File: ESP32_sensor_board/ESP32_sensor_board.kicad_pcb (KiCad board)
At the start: 4 copper layers, 112 x 56.5 mm, 83 parts, among them J1 SS-52400-003, J2 B2B-PH-SM4-TB, J3 GSD090012SEU, J4 Conn_01x04_Pin, J6 Conn_01x05_Pin, Q1 TEMT6000X01, Q2 BC817, Q3 BC817, U1 MCP73871, U2 BME280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

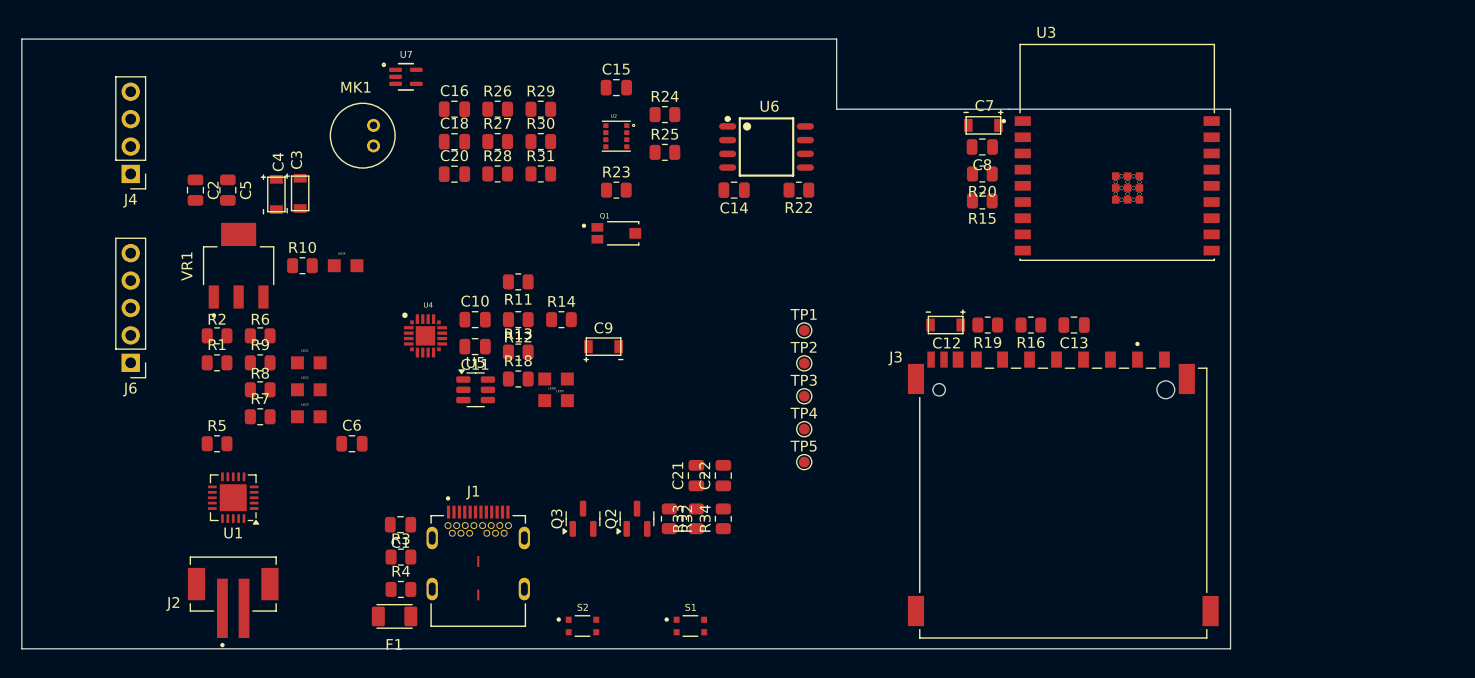
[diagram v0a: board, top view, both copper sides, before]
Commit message: Schematic design C19 added
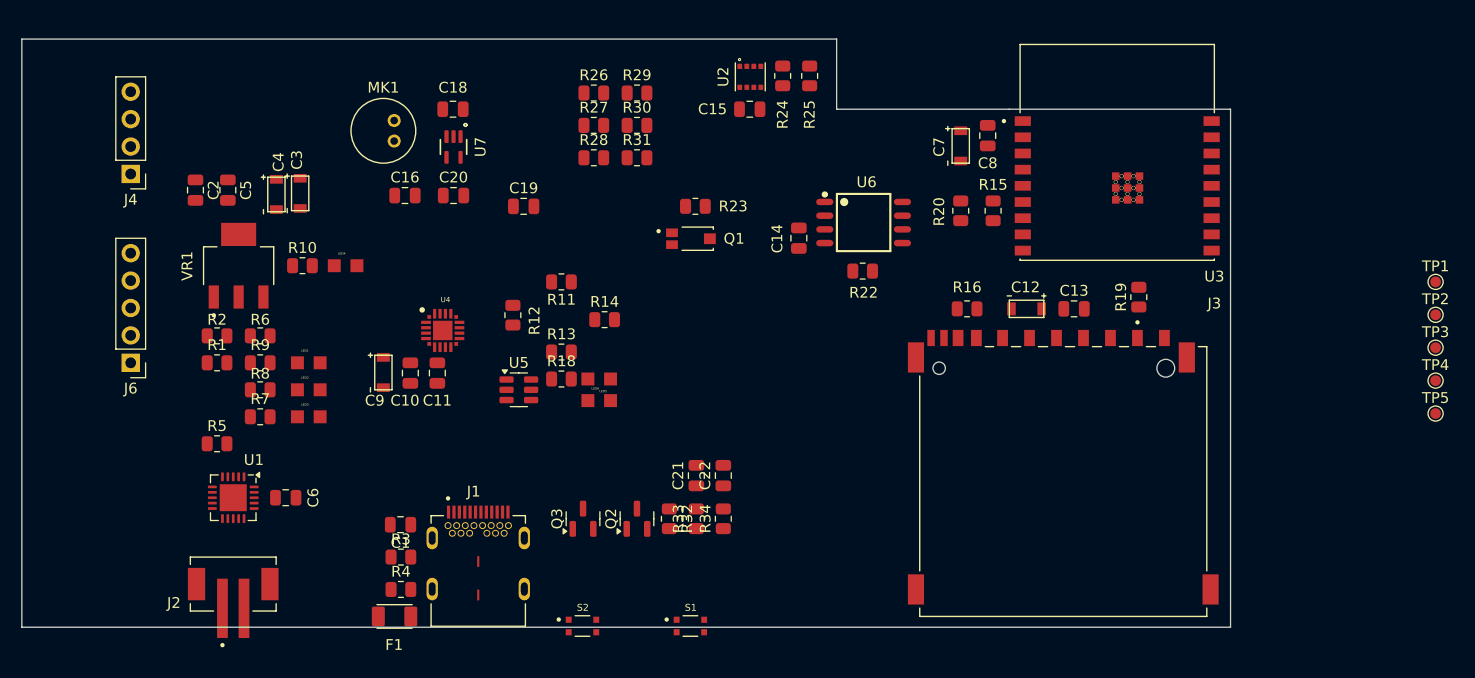
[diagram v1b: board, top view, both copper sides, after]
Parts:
- added C19: 1u, Capacitor_SMD:C_0805_2012Metric, F.Cu at (146.5, 75.5)
- moved TP1 58.7 mm to (231.0, 82.5)
- moved TP2 58.7 mm to (231.0, 85.5)
- moved TP3 58.7 mm to (231.0, 88.6)
- moved TP4 58.7 mm to (231.0, 91.7)
- moved TP5 58.7 mm to (231.0, 94.7)
- moved C9 19.6 mm to (132.7, 89.3), turned to -90 degrees
- moved R25 15.2 mm to (173.0, 63.4), turned to 90 degrees
- moved R19 14.2 mm to (203.5, 83.9), turned to 90 degrees
- moved U2 13.6 mm to (167.5, 63.5), turned to 90 degrees
- moved C15 12.5 mm to (167.4, 66.5)
- moved R24 11.5 mm to (170.5, 63.4), turned to 90 degrees
- moved U6 11.4 mm to (178.0, 77.0)
- moved R22 9.55 mm to (177.9, 81.5)
- moved C16 9.22 mm to (135.5, 74.5)
- moved R26 9.04 mm to (153.0, 65.0)
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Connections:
- net /ESP32-C3-02/Sensors/FEEDBACK renamed /ESP32-C3-02/Sensors/FEEDBACK_1
- R30 pad 2: GND -> /ESP32-C3-02/Sensors/FEEDBACK_2
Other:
- board size 112 x 56.5 mm -> 112 x 54.5 mm

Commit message: Layout design section 2 completed
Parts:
- added C17: 10n, Capacitor_SMD:C_0805_2012Metric, F.Cu at (143.0, 76.5)
- added H1: MountingHole, MountingHole:MountingHole_2.5mm, F.Cu at (177.0, 85.0)
- added H2: MountingHole, MountingHole:MountingHole_2.5mm, F.Cu at (129.0, 73.5)
- added H3: MountingHole, MountingHole:MountingHole_2.5mm, F.Cu at (129.0, 89.5)
- C20: value 0.1u -> 100p
- moved J4 45.4 mm to (154.5, 63.0), turned to -90 degrees
- moved J6 40.3 mm to (140.0, 63.0), turned to -90 degrees
- moved C9 31.8 mm to (164.3, 92.7), turned to 90 degrees
- moved C2 31.4 mm to (141.5, 92.5), turned to 180 degrees
- moved R2 30.1 mm to (145.0, 101.0), turned to -90 degrees
- moved C1 28.0 mm to (162.5, 99.5), turned to -90 degrees
- moved C11 27.5 mm to (166.0, 91.0), turned to 90 degrees
- moved R1 26.8 mm to (142.5, 101.0), turned to -90 degrees
- moved C10 25.0 mm to (161.0, 91.0), turned to 90 degrees
- moved U1 24.4 mm to (143.5, 107.5), turned to 180 degrees
- moved R12 24.3 mm to (167.0, 97.0), turned to 0 degrees
- moved C3 24.2 mm to (142.7, 89.2), turned to 180 degrees
- moved Q3 24.0 mm to (176.0, 103.4)
- moved F1 23.0 mm to (150.5, 97.0)
- moved R6 22.4 mm to (140.0, 101.0), turned to -90 degrees
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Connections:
- MK1 pad OUT: /ESP32-C3-02/Sensors/MK_INPUT -> /ESP32-C3-02/Sensors/MK
- R27 pad 2: /ESP32-C3-02/Sensors/MK_INPUT -> /ESP32-C3-02/Sensors/MK_DC
- R28 pad 2: /ESP32-C3-02/Sensors/MK_INPUT -> /ESP32-C3-02/Sensors/MK
- R29 pad 1: /ESP32-C3-02/Sensors/MK_INPUT -> /ESP32-C3-02/Sensors/MK_DC
- U7 pad 1: /ESP32-C3-02/Sensors/MK_INPUT -> /ESP32-C3-02/Sensors/MK_DC
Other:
- board size 112 x 54.5 mm -> 87 x 54.5 mm

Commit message: Layout design section 3 in progress
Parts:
- moved TP5 57.0 mm to (177.5, 75.0)
- moved TP2 51.5 mm to (180.0, 92.5)
- moved TP1 51.4 mm to (180.0, 88.8)
- moved TP3 47.3 mm to (184.8, 78.8)
- moved TP4 24.6 mm to (207.5, 84.2)
- moved H1 14.3 mm to (170.0, 72.5)
- moved R32 8.37 mm to (167.5, 104.0)
- moved C14 6.67 mm to (171.5, 81.5)
- moved R22 6.67 mm to (177.5, 84.5)
- moved U6 6.67 mm to (177.5, 80.0)
- moved R16 6.52 mm to (181.0, 84.5)
- moved C15 0.50 mm to (166.5, 66.5)
- moved F1 0.50 mm to (150.0, 97.0)
- moved R24 0.50 mm to (169.5, 63.5)
- moved R25 0.50 mm to (172.0, 63.5)
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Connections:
- net Net-(J1-CC1) renamed /CC1
- net Net-(J1-CC2) renamed /CC2
- TP3 pad 1: /ESP32-C3-02/SCLK -> /ESP32-C3-02/CLK
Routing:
- net /ESP32-C3-02/SCL: track 0.00 -> 76.4 mm, vias 0 -> 2
- net /ESP32-C3-02/SDA: track 0.00 -> 76.3 mm, vias 0 -> 2
- net /ESP32-C3-02/MISO_DO: track 0.00 -> 64.2 mm, vias 0 -> 2
- net /ESP32-C3-02/MOSI_DI: track 0.00 -> 56.3 mm
- net /ESP32-C3-02/CS_MEM: track 0.00 -> 43.2 mm, vias 0 -> 2
- net /ESP32-C3-02/CS_SD: track 0.00 -> 26.1 mm, vias 0 -> 2
- net /ESP32-C3-02/CLK: track 0.00 -> 23.2 mm
- net /VBAT: track 0.00 -> 12.0 mm
- net /ESP32-C3-02/DAT0: track 0.00 -> 9.35 mm
- net /ESP32-C3-02/DO: track 0.00 -> 7.40 mm
- net /ESP32-C3-02/SCLK: track 0.00 -> 7.00 mm
- net /ESP32-C3-02/USB_D+: track 0.00 -> 4.61 mm
- net /ESP32-C3-02/USB_D-: track 0.00 -> 4.61 mm
- net /USB_DP: track 0.00 -> 3.03 mm
- net /USB_DN: track 0.00 -> 3.03 mm
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- added copper zone on F.Cu, net +3.3V
- added copper zone on In1.Cu, net +3.3V
- added copper zone on F.Cu, net +5V
- added copper zone on F.Cu, net /+5V_USB
- added copper zone on In1.Cu, net /+5V_USB
- added copper zone on F.Cu, net /VBAT
- added copper zone on F.Cu, net /VBUS
- added copper zone on In1.Cu, net /VBUS
- added copper zone on F.Cu, net GND
- added copper zone on In2.Cu, net GND

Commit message: Layout design section 3 completed
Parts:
- moved TP4 2.15 mm to (206.2, 82.5)
- moved C1 1.68 mm to (161.8, 98.0), turned to 90 degrees
- moved C6 0.50 mm to (143.5, 112.0)
- moved LED1 0.50 mm to (128.0, 97.5)
- moved LED2 0.50 mm to (131.5, 97.5)
- moved LED3 0.50 mm to (135.0, 97.5)
- moved R1 0.50 mm to (142.5, 101.5)
- moved R2 0.50 mm to (145.0, 101.5)
- moved R5 0.50 mm to (137.5, 101.5)
- moved R6 0.50 mm to (140.0, 101.5)
- moved R7 0.50 mm to (135.0, 101.5)
- moved R8 0.50 mm to (131.5, 101.5)
- moved R9 0.50 mm to (128.0, 101.5)
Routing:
- net +5V: track 0.00 -> 33.4 mm
- net GND: track 0.00 -> 32.6 mm, vias 19 -> 35
- net +3.3V: track 0.00 -> 15.6 mm, vias 7 -> 13
- net /VBUS: track 0.00 -> 14.4 mm, vias 3 -> 8
- net /+5V_USB: track 0.00 -> 14.2 mm, vias 3 -> 11
- net /ESP32-C3-02/CS_MEM: track 43.2 -> 41.2 mm
- net /ESP32-C3-02/MISO_DO: track 64.2 -> 65.2 mm, vias 2 -> 0
- net /VBAT: track 12.0 -> 12.9 mm
- net /ESP32-C3-02/SCL: track 76.4 -> 77.1 mm, vias 2 -> 4
- net /ESP32-C3-02/CS_SD: track 26.1 -> 26.4 mm, vias 2 -> 0

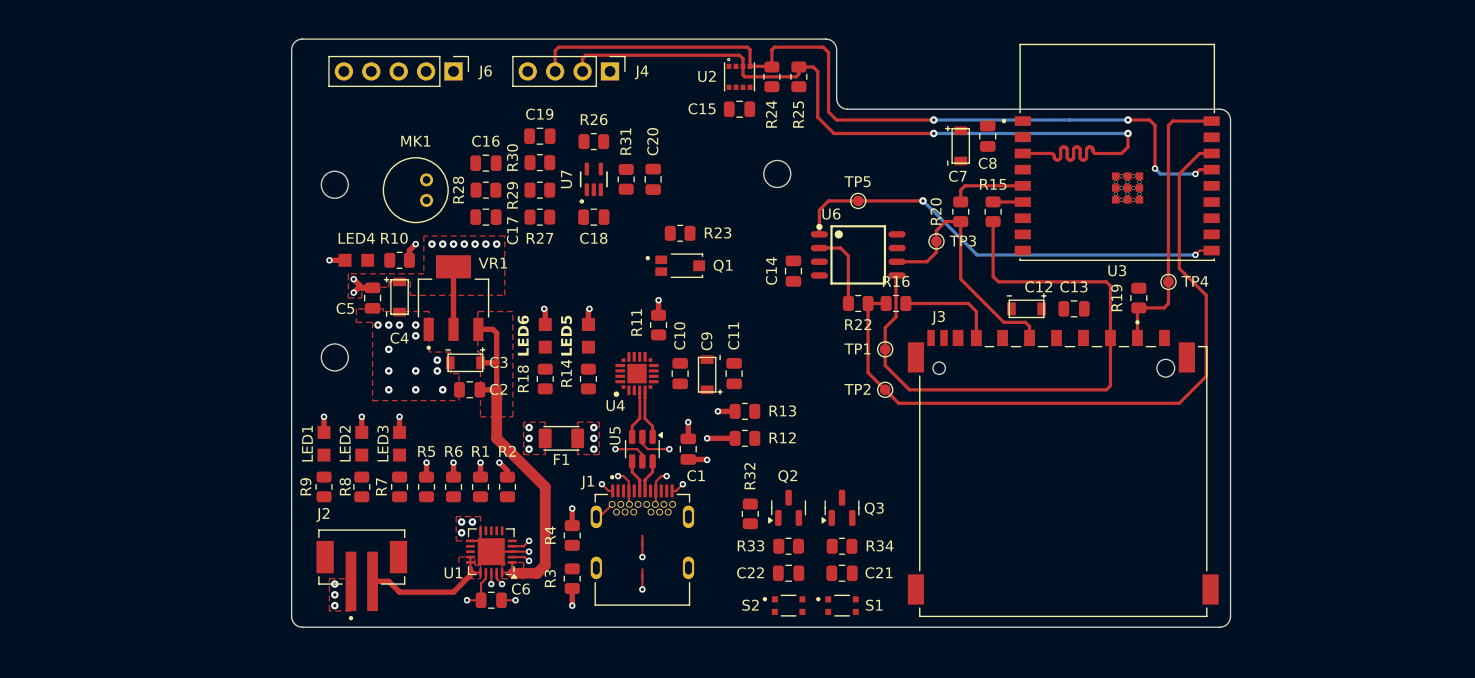
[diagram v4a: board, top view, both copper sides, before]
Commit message: Layout design section 4 completed
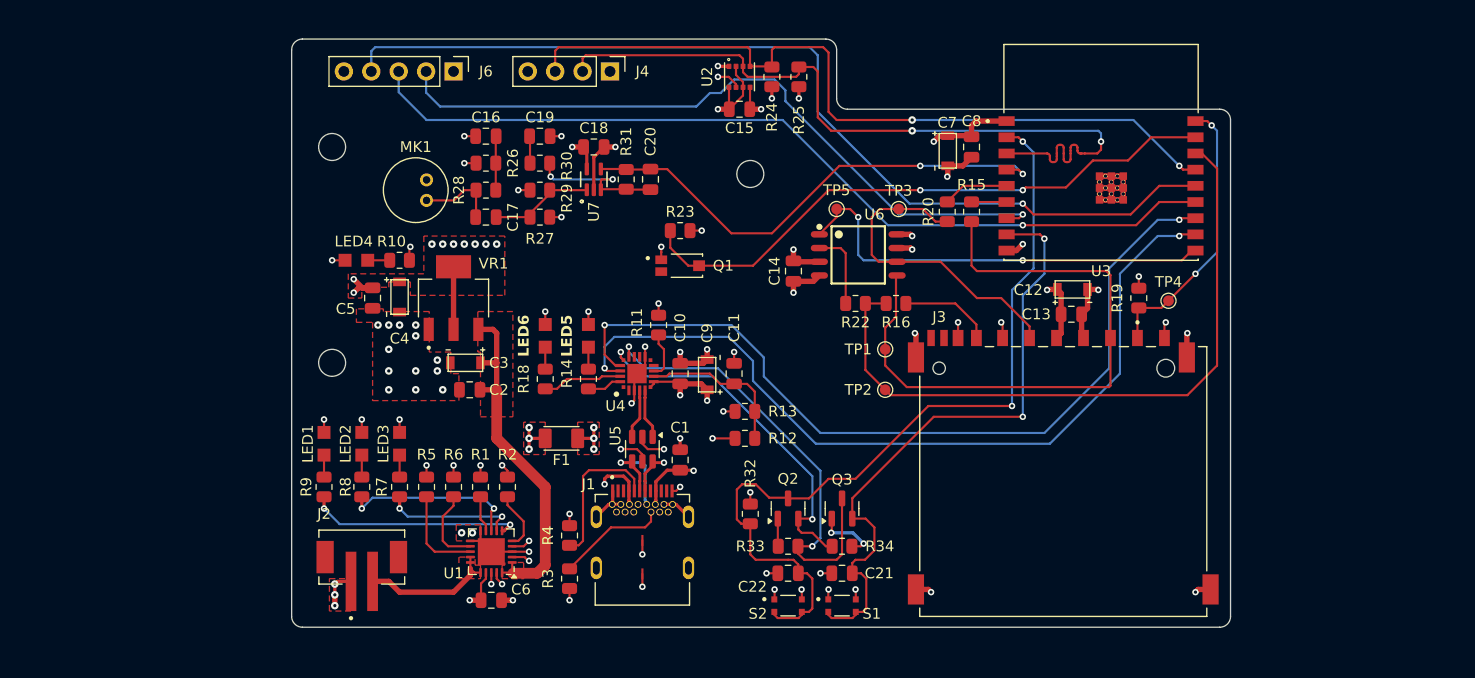
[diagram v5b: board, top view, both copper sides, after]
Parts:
- moved R26 10.2 mm to (143.0, 71.5), turned to 0 degrees
- moved C18 6.50 mm to (153.0, 70.0)
- moved TP3 4.61 mm to (181.2, 75.8)
- moved H2 3.51 mm to (128.8, 70.0)
- moved C16 2.50 mm to (143.0, 69.0), turned to 0 degrees
- moved H1 2.50 mm to (167.5, 72.5)
- moved TP5 2.14 mm to (175.5, 75.8)
- moved R15 2.00 mm to (188.0, 76.0)
- moved C8 1.80 mm to (188.0, 70.0)
- moved TP4 1.75 mm to (206.2, 84.2)
- moved U3 1.50 mm to (200.0, 70.5)
- moved C7 1.28 mm to (185.0, 68.8)
- moved C1 1.25 mm to (161.0, 99.0)
- moved R20 1.25 mm to (185.8, 76.0)
- moved C12 1.07 mm to (195.8, 84.0), turned to 0 degrees
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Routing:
- net /ESP32-C3-02/GPIO_19: track 0.00 -> 89.0 mm, vias 0 -> 1
- net /ESP32-C3-02/GPIO_18: track 0.00 -> 81.7 mm, vias 0 -> 1
- net /ESP32-C3-02/EN: track 0.00 -> 78.6 mm, vias 0 -> 2
- net /ESP32-C3-02/RX_TX: track 0.00 -> 78.5 mm, vias 0 -> 2
- net /ESP32-C3-02/TX_RX: track 0.00 -> 77.3 mm, vias 0 -> 2
- net GND: track 32.6 -> 108.5 mm, vias 35 -> 63
- net /ESP32-C3-02/GPIO_8: track 0.00 -> 66.2 mm, vias 0 -> 1
- net /ESP32-C3-02/BOOT: track 0.00 -> 58.5 mm, vias 0 -> 2
- net /ESP32-C3-02/PHOTO_C: track 0.00 -> 55.7 mm, vias 0 -> 2
- net /ESP32-C3-02/MIC_OUT: track 0.00 -> 46.2 mm, vias 0 -> 2
- net +3.3V: track 15.6 -> 61.6 mm, vias 13 -> 29
- net /ESP32-C3-02/DTR: track 0.00 -> 42.8 mm, vias 0 -> 2
- net /ESP32-C3-02/RTS: track 0.00 -> 33.8 mm, vias 0 -> 2
- net /CHARGING: track 0.00 -> 19.9 mm, vias 0 -> 2
- net /CHARGED: track 0.00 -> 16.3 mm, vias 0 -> 2
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- added copper zone on In2.Cu, net +3.3V
- added copper zone on In2.Cu, net /+5V_USB
- added copper zone on In2.Cu, net /VBUS
- added copper zone on In1.Cu, net GND
- removed copper zone on In1.Cu, net +3.3V
- removed copper zone on In1.Cu, net /+5V_USB
- removed copper zone on In1.Cu, net /VBUS
- removed copper zone on In2.Cu, net GND

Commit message: Production section completed
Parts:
- moved H2 2.50 mm to (128.8, 72.5)
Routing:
- net +3.3V: track 61.6 -> 60.7 mm
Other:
- board text added: "08"
- board text added: "18"
- board text added: "19"
- board text added: "3V3"
- board text added: "BME280"
- board text added: "CHARGED"
- board text added: "CHARGER"
- board text added: "CHARGING"
- board text added: "FLASH"
- board text added: "GND"
- board text added: "LIGHT SENSOR"
- board text added: "POWER"
- board text added: "PWR OK"
- board text added: "RESET & BOOT"
- board text added: "SCL"
- board text added: "SDA"
- board text added: "SOUND"
- board text added: "USB"

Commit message: Prototype 2 completed
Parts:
- added C23: 0.1u, Capacitor_SMD:C_0805_2012Metric, F.Cu at (157.2, 79.8)
- added C24: 10n, Capacitor_SMD:C_0805_2012Metric, F.Cu at (165.8, 80.2)
- added C25: 10n, Capacitor_SMD:C_0805_2012Metric, F.Cu at (212.2, 70.0)
- added F2: 0ZCJ0110FF2E, footprints:RESC3216X125N, F.Cu at (144.2, 96.5)
- added R17: 35WR100KLFTR, footprints:TRIM_35WR100KLFTR, F.Cu at (151.8, 80.0)
- C19: value 1u -> 10u
- C20: value 100p -> 0.1u
- R30: value 10K -> 1K
- R31: value 100K -> 22K
- S1, S2: value USLPT2819DT2TR -> TL3305AF260QG; footprint footprints:SW_USLPT2819DT2TR -> footprints:SW_TL3305AF260QG
- moved R34 8.81 mm to (172.9, 98.8)
- moved R12 4.37 mm to (163.0, 95.2)
- moved S2 3.48 mm to (167.8, 111.2), turned to -90 degrees
- moved C22 3.20 mm to (168.5, 107.5), turned to 0 degrees
- moved R4 2.51 mm to (150.5, 103.5)
- moved R33 2.47 mm to (172.8, 105.2)
- moved C21 2.24 mm to (177.0, 107.5)
- moved S1 2.15 mm to (177.8, 111.2), turned to -90 degrees
- moved Q3 1.68 mm to (175.2, 102.0), turned to 0 degrees
- moved R32 1.60 mm to (168.5, 105.2), turned to 0 degrees
- moved Q2 1.58 mm to (170.5, 102.0), turned to 180 degrees
- moved C12 1.25 mm to (196.9, 83.5)
- moved C13 1.25 mm to (198.5, 85.5)
- moved J3 1.25 mm to (197.8, 101.0)
- moved LED5 1.25 mm to (151.2, 87.5)
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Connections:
- Q1 pad 1: GND -> /ESP32-C3-02/PHOTO_C
- Q1 pad 3: /ESP32-C3-02/PHOTO_C -> +3.3V
- Q3 pad 2: /ESP32-C3-02/BOOT -> /ESP32-C3-02/DTR
- Q3 pad 3: /ESP32-C3-02/DTR -> /ESP32-C3-02/BOOT
- R23 pad 1: +3.3V -> /ESP32-C3-02/PHOTO_C
- R23 pad 2: /ESP32-C3-02/PHOTO_C -> GND
- R31 pad 2: /ESP32-C3-02/MIC_OUT -> /ESP32-C3-02/Sensors/FEEDBACK_3
- S1 pad 1: GND -> /ESP32-C3-02/BOOT
- S1 pad 2: GND -> /ESP32-C3-02/BOOT
- S1 pad 3: /ESP32-C3-02/BOOT -> GND
- S1 pad 4: /ESP32-C3-02/BOOT -> GND
- S2 pad 1: GND -> /ESP32-C3-02/EN
- S2 pad 2: GND -> /ESP32-C3-02/EN
- S2 pad 3: /ESP32-C3-02/EN -> GND
- S2 pad 4: /ESP32-C3-02/EN -> GND
- U1 pad 1: +5V -> /OUT
- U1 pad 20: +5V -> /OUT
- U3 pad 18: /ESP32-C3-02/CS_SD -> /ESP32-C3-02/MIC_OUT
- U3 pad 4: /ESP32-C3-02/MIC_OUT -> /ESP32-C3-02/CS_SD
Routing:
- net /ESP32-C3-02/MIC_OUT: track 46.2 -> 80.8 mm
- net +5V: track 33.4 -> 10.1 mm
- net /OUT: track 0.00 -> 18.4 mm
- net /ESP32-C3-02/CS_SD: track 25.9 -> 36.9 mm
- net /ESP32-C3-02/PHOTO_C: track 55.7 -> 65.3 mm
- net /ESP32-C3-02/DTR: track 42.8 -> 33.8 mm
- net /ESP32-C3-02/RTS: track 33.8 -> 25.0 mm
- net /ESP32-C3-02/Sensors/FEEDBACK_3: track 0.00 -> 8.74 mm, vias 0 -> 2
- net GND: track 108.5 -> 116.9 mm, vias 63 -> 66
- net +3.3V: track 60.7 -> 64.3 mm
- net /ESP32-C3-02/EN: track 78.6 -> 75.0 mm
- net /ESP32-C3-02/User interface/B_Q3: track 5.94 -> 2.50 mm, vias 2 -> 0
- net /CC1: track 13.9 -> 11.6 mm
- net /ESP32-C3-02/GPIO_19: track 89.0 -> 90.7 mm
- net /ESP32-C3-02/BOOT: track 58.5 -> 60.1 mm
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- added copper zone on F.Cu, net /OUT
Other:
- board size 87 x 54.5 mm -> 89 x 54.5 mm
- board text added: "BOOT"
- board text added: "EN"
- board text added: "LIGHT"
- board text added: "RX"
- board text added: "TX"
- board text removed: "LIGHT SENSOR"
- board text removed: "RESET & BOOT"
